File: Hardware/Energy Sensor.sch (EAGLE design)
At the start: 21 parts

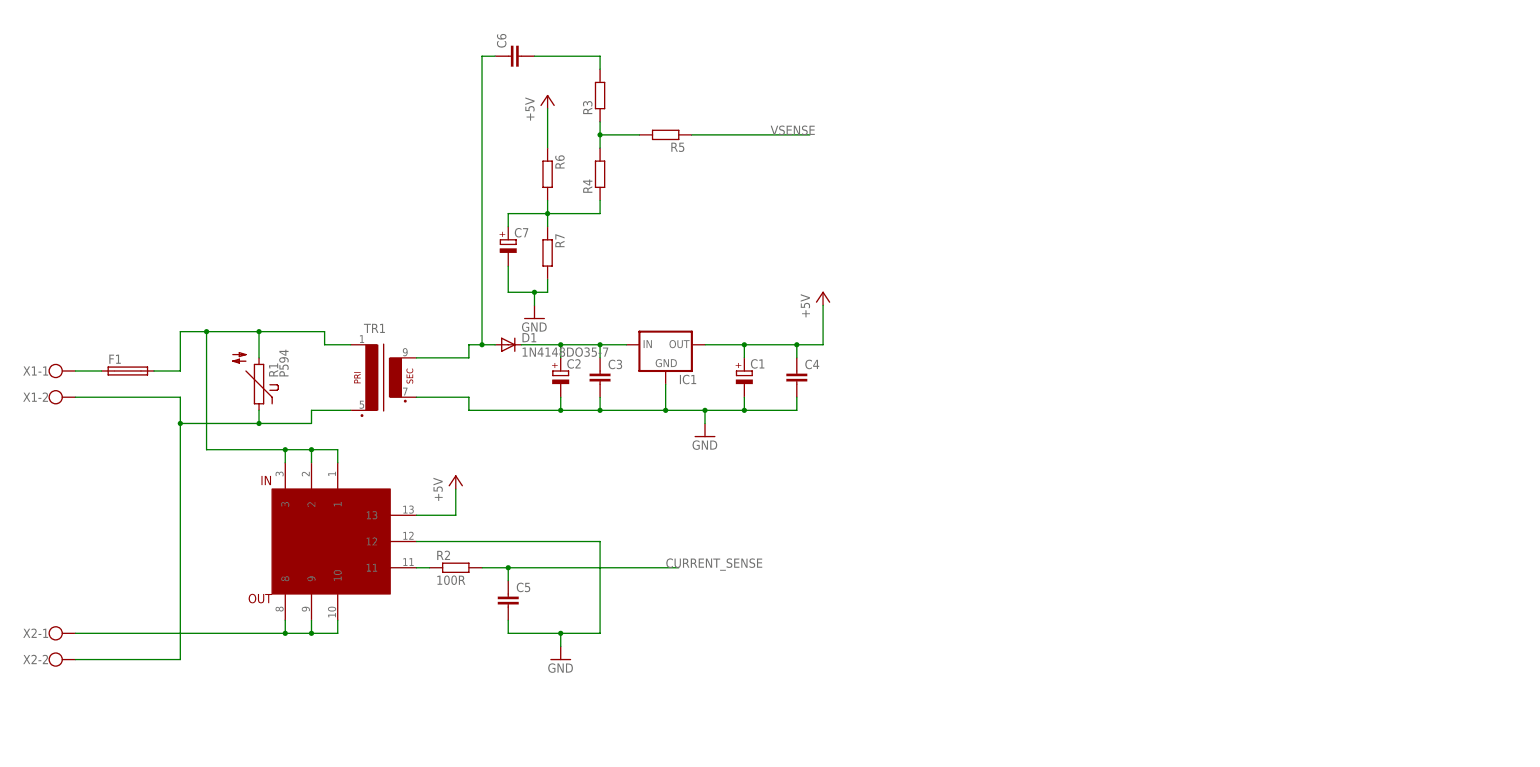
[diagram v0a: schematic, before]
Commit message: initial mock up of board. still need to check silkscreen arrangement
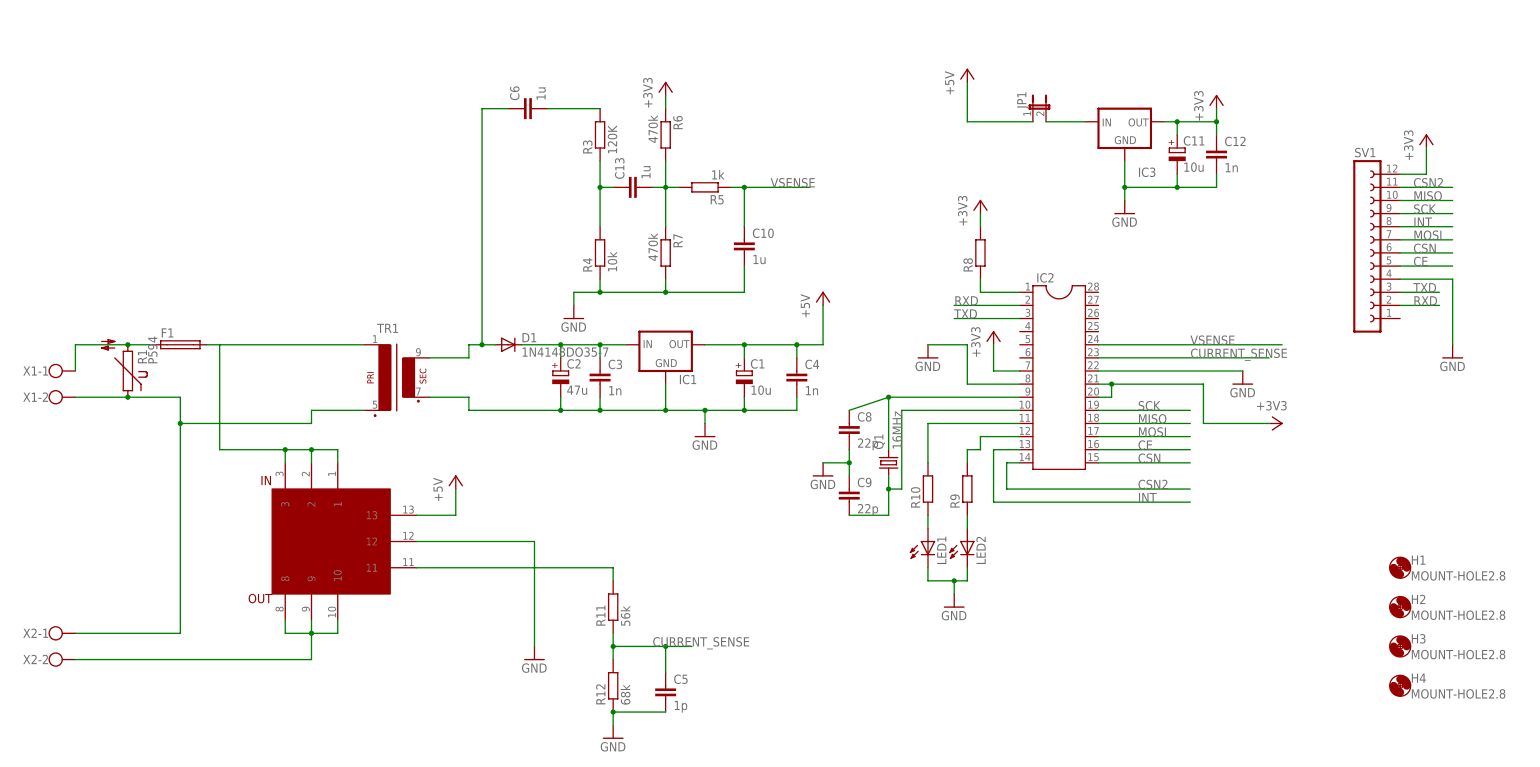
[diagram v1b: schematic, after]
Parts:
- removed C7: (no value), rcl:CPOL-EU140CLH-1010
- removed R2: 100R, rcl:R-EU_0207/7
- added C10, C13: 1u, rcl:C-EU025-025X050
- added C11: 10u, rcl:CPOL-EUE2.5-6
- added C12: 1n, rcl:C-EU025-025X050
- added C8, C9: 22p, rcl:C-EU025-025X050
- added H1, H2, H3, H4: MOUNT-HOLE2.8, holes:MOUNT-HOLE2.8
- added IC2: (no value), ic-package:DIL28-4
- added IC3: (no value), v-reg:79XXL
- added JP1: (no value), jumper:JP1E
- added LED1, LED2: (no value), led:LED5MM
- added Q1: 16MHz, crystal:CRYSTALHC49S
- added R10, R8, R9: (no value), rcl:R-EU_0207/7
- added R11: 56k, rcl:R-EU_0207/7
- added R12: 68k, rcl:R-EU_0207/7
- added SV1: (no value), con-lsta:FE12W
- C1: value (none) -> 10u; device rcl:CPOL-EU140CLH-1010 -> rcl:CPOL-EUE2.5-6
- C2: value (none) -> 47u; device rcl:CPOL-EU140CLH-1010 -> rcl:CPOL-EUE2.5-6
- C3, C4: value (none) -> 1n; device rcl:C-EU050-025X075 -> rcl:C-EU025-025X050
- C5: value (none) -> 1p; device rcl:C-EU050-025X075 -> rcl:C-EU025-025X050
- C6: value (none) -> 1u; device rcl:C-EU050-025X075 -> rcl:C-EU025-025X050
- R3: value (none) -> 120K
- R4: value (none) -> 10k
- R5: value (none) -> 1k
- R6, R7: value (none) -> 470k
- TR1: device trafo:VV11 -> xformer:VV11
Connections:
- new net +3V3: C11.+, C12.1, IC2.20, IC2.21, IC2.7, IC3.OUT, R6.1, R8.2, SV1.12
- new net CE: IC2.16, SV1.5
- new net CSN: IC2.15, SV1.6
- new net CSN2: IC2.14, SV1.11
- new net INT: IC2.13, SV1.8
- new net MISO: IC2.18, SV1.10
- new net MOSI: IC2.17, SV1.7
- new net N$11: R11.2, U$1.11
- new net N$12: C8.1, IC2.9, Q1.2
- new net N$13: C9.2, IC2.10, Q1.1
- new net N$14: LED1.A, R10.1
- new net N$15: LED2.A, R9.1
- new net N$16: IC2.1, R8.1
- new net N$17: IC2.12, R9.2
- new net N$18: IC2.11, R10.2
- new net RXD: IC2.2, SV1.2
- new net SCK: IC2.19, SV1.9
- new net TXD: IC2.3, SV1.3
- net +5V: now also JP1.1; no longer R6.1
- net CURRENT_SENSE: now also IC2.23, R11.1, R12.2; no longer R2.2
- net GND: now also C10.2, C11.-, C12.2, C8.2, C9.1, IC2.22, IC2.8, IC3.GND, LED1.C, LED2.C, R12.1, R4.1, SV1.4; no longer C7.-
- net N$1: now also R1.2
- net N$10: now also C13.2, R5.2; no longer C7.+, R4.1
- net N$2: now also X2-1.KL; no longer X2-2.KL
- net N$3: now also IC3.IN, JP1.2; no longer R2.1, U$1.11
- net N$6: no longer R1.2
- net N$8: now also X2-2.KL; no longer X2-1.KL
- net N$9: now also C13.1; no longer R5.2
- net VSENSE: now also C10.1, IC2.24
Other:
- moved on the sheet: C5, C6, F1, R1, R3, R4, R5, R6, R7, TR1

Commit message: update schematics, added switchmode psu to heating controller. fixed line endings for existing files
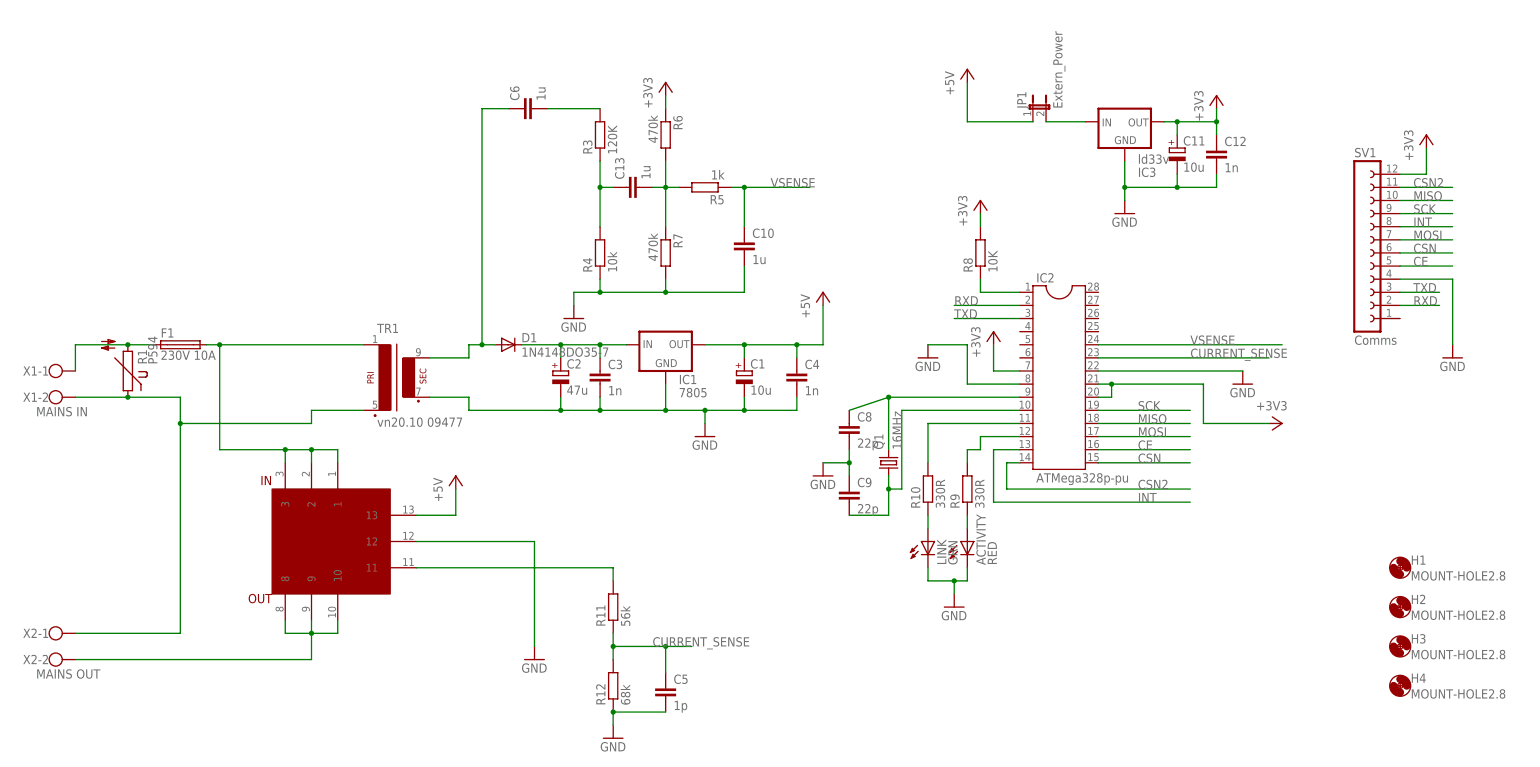
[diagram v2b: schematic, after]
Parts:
- ACTIVITY: value (none) -> RED
- F1: value (none) -> 230V 10A
- IC1: value (none) -> 7805
- IC2: value (none) -> ATMega328p-pu
- IC3: value (none) -> ld33v
- JP1: value (none) -> Extern_Power
- LINK: value (none) -> GRN
- R10, R9: value (none) -> 330R
- R8: value (none) -> 10K
- SV1: value (none) -> Comms
- TR1: value (none) -> vn20.10 09477
- X1: value (none) -> MAINS IN
- X2: value (none) -> MAINS OUT
- renumbered LED1 to LINK, LED2 to ACTIVITY
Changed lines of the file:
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@@
 <part name="C1" library="rcl" deviceset="CPOL-EU" device="E2.5-6" value="10u"/>
 <part name="C2" library="rcl" deviceset="CPOL-EU" device="E2.5-6" value="47u"/>
-<part name="X1" library="con-wago-500" deviceset="W237-102" device=""/>
-<part name="X2" library="con-wago-500" deviceset="W237-102" device=""/>
+<part name="X1" library="con-wago-500" deviceset="W237-102" device="" value="MAINS IN"/>
+<part name="X2" library="con-wago-500" deviceset="W237-102" device="" value="MAINS OUT"/>
 <part name="R1" library="varistor" deviceset="P594" device=""/>
-<part name="F1" library="fuse" deviceset="GSH15" device=""/>
-<part name="TR1" library="xformer" deviceset="VV11" device=""/>
+<part name="F1" library="fuse" deviceset="GSH15" device="" value="230V 10A"/>
+<part name="TR1" library="xformer" deviceset="VV11" device="" value="vn20.10 09477"/>
 <part name="D1" library="diode" deviceset="1N4148" device="DO35-7"/>
-<part name="IC1" library="v-reg" deviceset="78XXL" device=""/>
+<part name="IC1" library="v-reg" deviceset="78XXL" device="" value="7805"/>
 <part name="C3" library="rcl" deviceset="C-EU" device="025-025X050" value="1n"/>
 <part name="C4" library="rcl" deviceset="C-EU" device="025-025X050" value="1n"/>
@@
 <part name="R7" library="rcl" deviceset="R-EU_" device="0207/7" value="470k"/>
 <part name="GND3" library="supply1" deviceset="GND" device=""/>
-<part name="IC2" library="ic-package" deviceset="DIL28" device="-4"/>
+<part name="IC2" library="ic-package" deviceset="DIL28" device="-4" value="ATMega328p-pu"/>
 <part name="GND4" library="supply1" deviceset="GND" device=""/>
 <part name="Q1" library="crystal" deviceset="CRYSTAL" device="HC49S" value="16MHz"/>
-<part name="R8" library="rcl" deviceset="R-EU_" device="0207/7"/>
+<part name="R8" library="rcl" deviceset="R-EU_" device="0207/7" value="10K"/>
 <part name="C8" library="rcl" deviceset="C-EU" device="025-025X050" value="22p"/>
 <part name="C9" library="rcl" deviceset="C-EU" device="025-025X050" value="22p"/>
@@
 <part name="GND5" library="supply1" deviceset="GND" device=""/>
 <part name="GND6" library="supply1" deviceset="GND" device=""/>
-<part name="SV1" library="con-lsta" deviceset="FE12W" device=""/>
+<part name="SV1" library="con-lsta" deviceset="FE12W" device="" value="Comms"/>
 <part name="GND7" library="supply1" deviceset="GND" device=""/>
 <part name="P+7" library="supply1" deviceset="+5V" device=""/>
 <part name="+3V1" library="supply1" deviceset="+3V3" device=""/>
-<part name="IC3" library="v-reg" deviceset="79XXL" device=""/>
+<part name="IC3" library="v-reg" deviceset="79XXL" device="" value="ld33v"/>
 <part name="GND8" library="supply1" deviceset="GND" device=""/>
 <part name="+3V2" library="supply1" deviceset="+3V3" device=""/>
@@
 <part name="C11" library="rcl" deviceset="CPOL-EU" device="E2.5-6" value="10u"/>
 <part name="C12" library="rcl" deviceset="C-EU" device="025-025X050" value="1n"/>
-<part name="LED1" library="led" deviceset="LED" device="5MM"/>
-<part name="LED2" library="led" deviceset="LED" device="5MM"/>
-<part name="R9" library="rcl" deviceset="R-EU_" device="0207/7"/>
-<part name="R10" library="rcl" deviceset="R-EU_" device="0207/7"/>
+<part name="LINK" library="led" deviceset="LED" device="5MM" value="GRN"/>
+<part name="ACTIVITY" library="led" deviceset="LED" device="5MM" value="RED"/>
+<part name="R9" library="rcl" deviceset="R-EU_" device="0207/7" value="330R"/>
+<part name="R10" library="rcl" deviceset="R-EU_" device="0207/7" value="330R"/>
 <part name="GND9" library="supply1" deviceset="GND" device=""/>
 <part name="R11" library="rcl" deviceset="R-EU_" device="0207/7" value="56k"/>
@@
 <part name="+3V6" library="supply1" deviceset="+3V3" device=""/>
 <part name="C13" library="rcl" deviceset="C-EU" device="025-025X050" value="1u"/>
-<part name="JP1" library="jumper" deviceset="JP1E" device=""/>
+<part name="JP1" library="jumper" deviceset="JP1E" device="" value="Extern_Power"/>
 <part name="H1" library="holes" deviceset="MOUNT-HOLE" device="2.8"/>
 <part name="H2" library="holes" deviceset="MOUNT-HOLE" device="2.8"/>
@@
 <instance part="C11" gate="G$1" x="198.12" y="121.92"/>
 <instance part="C12" gate="G$1" x="205.74" y="121.92"/>
-<instance part="LED1" gate="G$1" x="149.86" y="45.72"/>
-<instance part="LED2" gate="G$1" x="157.48" y="45.72"/>
+<instance part="LINK" gate="G$1" x="149.86" y="45.72"/>
+<instance part="ACTIVITY" gate="G$1" x="157.48" y="45.72"/>
 <instance part="R9" gate="G$1" x="157.48" y="55.88" rot="R90"/>
 <instance part="R10" gate="G$1" x="149.86" y="55.88" rot="R90"/>
@@
 </segment>
 <segment>
-<pinref part="LED2" gate="G$1" pin="C"/>
+<pinref part="ACTIVITY" gate="G$1" pin="C"/>
 <wire x1="157.48" y1="40.64" x2="157.48" y2="38.1" width="0.1524" layer="91"/>
 <wire x1="157.48" y1="38.1" x2="154.94" y2="38.1" width="0.1524" layer="91"/>
 <pinref part="GND9" gate="1" pin="GND"/>
 <wire x1="154.94" y1="38.1" x2="154.94" y2="35.56" width="0.1524" layer="91"/>
-<pinref part="LED1" gate="G$1" pin="C"/>
+<pinref part="LINK" gate="G$1" pin="C"/>
 <wire x1="149.86" y1="40.64" x2="149.86" y2="38.1" width="0.1524" layer="91"/>
 <wire x1="149.86" y1="38.1" x2="154.94" y2="38.1" width="0.1524" layer="91"/>
@@
 <pinref part="TR1" gate="1" pin="P1"/>
 <wire x1="40.64" y1="83.82" x2="12.7" y2="83.82" width="0.1524" layer="91"/>
+<junction x="12.7" y="83.82"/>
 </segment>
 </net>
@@
 <segment>
 <pinref part="R10" gate="G$1" pin="1"/>
-<pinref part="LED1" gate="G$1" pin="A"/>
+<pinref part="LINK" gate="G$1" pin="A"/>
 <wire x1="149.86" y1="50.8" x2="149.86" y2="48.26" width="0.1524" layer="91"/>
 </segment>
@@
 <segment>
 <pinref part="R9" gate="G$1" pin="1"/>
-<pinref part="LED2" gate="G$1" pin="A"/>
+<pinref part="ACTIVITY" gate="G$1" pin="A"/>
 <wire x1="157.48" y1="50.8" x2="157.48" y2="48.26" width="0.1524" layer="91"/>
 </segment>

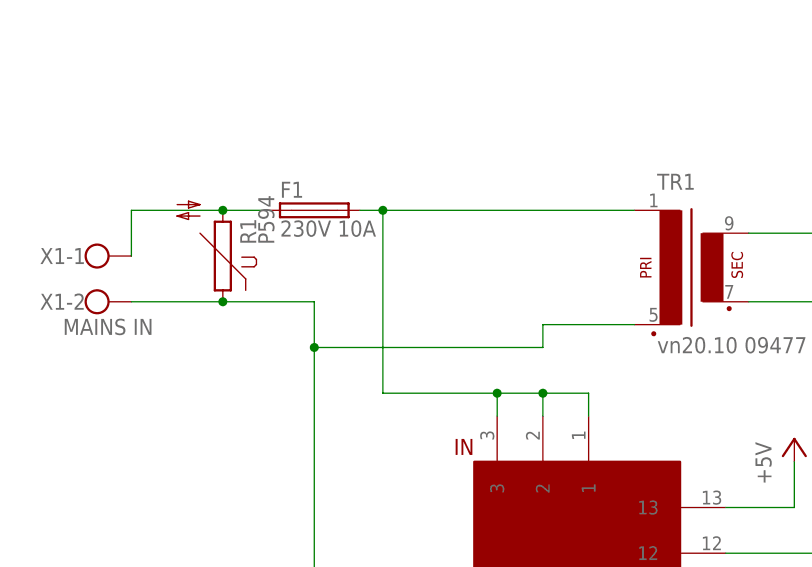
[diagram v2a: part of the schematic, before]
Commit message: updated fuse locations and updated missing values
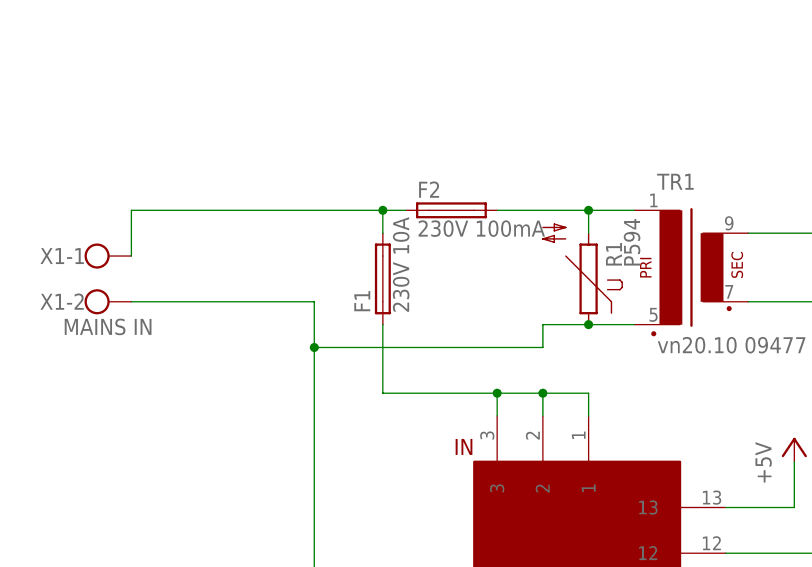
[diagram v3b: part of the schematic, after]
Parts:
- added F2: 230V 100mA, fuse:GSH15
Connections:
- removed net N$1: F1.1, R1.2, X1-1.KL
- new net N$19: F2.2, R1.2, TR1.P1
- new net N$22: F1.2, F2.1, X1-1.KL
- net N$6: now also F1.1; no longer F1.2, TR1.P1
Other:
- moved on the sheet: F1, R1
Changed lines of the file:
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@@
 <?xml version="1.0" encoding="utf-8"?>
 <!DOCTYPE eagle SYSTEM "eagle.dtd">
-<eagle version="6.4">
+<eagle version="6.5.0">
 <drawing>
 <settings>
@@
 <part name="H3" library="holes" deviceset="MOUNT-HOLE" device="2.8"/>
 <part name="H4" library="holes" deviceset="MOUNT-HOLE" device="2.8"/>
+<part name="F2" library="fuse" deviceset="GSH15" device="" value="230V 100mA"/>
 </parts>
 <sheets>
@@
 <instance part="X2" gate="-1" x="-20.32" y="27.94"/>
 <instance part="X2" gate="-2" x="-20.32" y="22.86"/>
-<instance part="R1" gate="1" x="-5.08" y="78.74" rot="R90"/>
-<instance part="F1" gate="1" x="5.08" y="83.82"/>
+<instance part="R1" gate="1" x="35.56" y="76.2" rot="R90"/>
+<instance part="F1" gate="1" x="12.7" y="76.2" rot="R90"/>
 <instance part="TR1" gate="1" x="45.72" y="78.74"/>
 <instance part="D1" gate="G$1" x="68.58" y="83.82"/>
@@
 <instance part="H3" gate="G$1" x="241.3" y="25.4"/>
 <instance part="H4" gate="G$1" x="241.3" y="17.78"/>
+<instance part="F2" gate="1" x="20.32" y="83.82"/>
 </instances>
 <busses>
 </busses>
 <nets>
-<net name="N$1" class="0">
-<segment>
-<pinref part="X1" gate="-1" pin="KL"/>
-<pinref part="F1" gate="1" pin="1"/>
-<wire x1="-15.24" y1="78.74" x2="-15.24" y2="83.82" width="0.1524" layer="91"/>
-<wire x1="-15.24" y1="83.82" x2="-5.08" y2="83.82" width="0.1524" layer="91"/>
-<pinref part="R1" gate="1" pin="2"/>
-<junction x="-5.08" y="83.82"/>
-<wire x1="-5.08" y1="83.82" x2="0" y2="83.82" width="0.1524" layer="91"/>
-</segment>
-</net>
 <net name="N$2" class="0">
 <segment>
-<pinref part="X1" gate="-2" pin="KL"/>
-<wire x1="-15.24" y1="73.66" x2="-5.08" y2="73.66" width="0.1524" layer="91"/>
-<wire x1="-5.08" y1="73.66" x2="5.08" y2="73.66" width="0.1524" layer="91"/>
 <wire x1="5.08" y1="73.66" x2="5.08" y2="68.58" width="0.1524" layer="91"/>
 <wire x1="5.08" y1="68.58" x2="30.48" y2="68.58" width="0.1524" layer="91"/>
@@
 <pinref part="X2" gate="-1" pin="KL"/>
 <wire x1="-15.24" y1="27.94" x2="5.08" y2="27.94" width="0.1524" layer="91"/>
+<pinref part="TR1" gate="1" pin="P2"/>
+<wire x1="30.48" y1="71.12" x2="35.56" y2="71.12" width="0.1524" layer="91"/>
 <pinref part="R1" gate="1" pin="1"/>
-<junction x="-5.08" y="73.66"/>
-<pinref part="TR1" gate="1" pin="P2"/>
-<wire x1="30.48" y1="71.12" x2="40.64" y2="71.12" width="0.1524" layer="91"/>
+<wire x1="35.56" y1="71.12" x2="40.64" y2="71.12" width="0.1524" layer="91"/>
+<junction x="35.56" y="71.12"/>
+<pinref part="X1" gate="-2" pin="KL"/>
+<wire x1="-15.24" y1="73.66" x2="5.08" y2="73.66" width="0.1524" layer="91"/>
 </segment>
 </net>
@@
 <wire x1="25.4" y1="60.96" x2="25.4" y2="63.5" width="0.1524" layer="91"/>
 <wire x1="25.4" y1="63.5" x2="30.48" y2="63.5" width="0.1524" layer="91"/>
-<pinref part="F1" gate="1" pin="2"/>
-<wire x1="10.16" y1="83.82" x2="12.7" y2="83.82" width="0.1524" layer="91"/>
-<wire x1="12.7" y1="83.82" x2="12.7" y2="63.5" width="0.1524" layer="91"/>
+<wire x1="12.7" y1="71.12" x2="12.7" y2="63.5" width="0.1524" layer="91"/>
 <wire x1="25.4" y1="63.5" x2="12.7" y2="63.5" width="0.1524" layer="91"/>
 <junction x="25.4" y="63.5"/>
 <junction x="30.48" y="63.5"/>
-<pinref part="TR1" gate="1" pin="P1"/>
-<wire x1="40.64" y1="83.82" x2="12.7" y2="83.82" width="0.1524" layer="91"/>
-<junction x="12.7" y="83.82"/>
+<pinref part="F1" gate="1" pin="1"/>
 </segment>
 </net>
@@
 </segment>
 </net>
+<net name="N$19" class="0">
+<segment>
+<pinref part="TR1" gate="1" pin="P1"/>
+<wire x1="40.64" y1="83.82" x2="35.56" y2="83.82" width="0.1524" layer="91"/>
+<pinref part="F2" gate="1" pin="2"/>
+<pinref part="R1" gate="1" pin="2"/>
+<wire x1="35.56" y1="83.82" x2="25.4" y2="83.82" width="0.1524" layer="91"/>
+<wire x1="35.56" y1="81.28" x2="35.56" y2="83.82" width="0.1524" layer="91"/>
+<junction x="35.56" y="83.82"/>
+</segment>
+</net>
+<net name="N$22" class="0">
+<segment>
+<pinref part="X1" gate="-1" pin="KL"/>
+<wire x1="-15.24" y1="78.74" x2="-15.24" y2="83.82" width="0.1524" layer="91"/>
+<pinref part="F2" gate="1" pin="1"/>
+<wire x1="15.24" y1="83.82" x2="12.7" y2="83.82" width="0.1524" layer="91"/>
+<wire x1="12.7" y1="83.82" x2="12.7" y2="81.28" width="0.1524" layer="91"/>
+<pinref part="F1" gate="1" pin="2"/>
+<wire x1="-15.24" y1="83.82" x2="12.7" y2="83.82" width="0.1524" layer="91"/>
+<junction x="12.7" y="83.82"/>
+</segment>
+</net>
